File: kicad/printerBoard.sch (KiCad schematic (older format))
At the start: 24 parts, among them U1 POLOLU_A4988, U2 POLOLU_A4988

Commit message: Adding USL - sensors...
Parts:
- removed P?: CONN_01X04, symbol CONN_01X04
- added P?: CONN_01X05, symbol CONN_01X05
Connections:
- net ADIR is gone; now on net YDIR: U2.16 (DIR), U?.26 (PB13/SPI2_SCK/TIM1_CH1N/USART3_CTS)
- net AENABLE is gone; now on net YENABLE: U2.9 (EN), U?.22 (PB11/ADC1_EXTI11/ADC2_EXTI11/I2C2_SDA/TIM2_CH4/USART3_RX)
- net ASTEP is gone; now on net YSTEP: U2.15 (STEP), U?.25 (PB12/I2C2_SMBA/SPI2_NSS/TIM1_BKIN/USART3_CK)
- net Bpin1: no longer U?.11 (ADC1_IN1/ADC2_IN1/TIM2_CH2/USART2_RTS/PA1)
- net ULN12: no longer P?.2 (P2)
- net YDIR: no longer U?.16 (DIR), U?.20 (PB2/BOOT1)
- net YENABLE: no longer U?.45 (PB8/CAN_RX/I2C1_SCL/TIM4_CH3), U?.9 (EN)
- net YOUT1A: now also P?.2 (P2), U2.4 (1A); no longer U?.4 (1A)
- net YOUT1B: now also P?.1 (P1), U2.3 (IB); no longer U?.3 (IB)
- net YOUT2A: now also P?.3 (P3), U2.5 (2A); no longer U?.5 (2A)
- net YOUT2B: now also P?.4 (P4), U2.6 (2B); no longer U?.6 (2B)
- net YSTEP: no longer U?.15 (STEP), U?.21 (PB10/I2C2_SCL/TIM2_CH3/USART3_TX)
- net Zpin2: no longer U?.41 (PB5/I2C1_SMBA/SPI1_MOSI/TIM3_CH2)
- net Extruder_Sensor: now reaches U?.10 (ADC1_IN0/ADC2_IN0/SYS_WKUP/TIM2_CH1/TIM2_ETR/USART2_CTS/PA0)
- net Extruder_Sensor: now also P?.16 (P16)
- net PA13: now reaches U?.34 (SYS_JTMS-SWDIO/PA13)
- net PA13: now also U?.6 (I6)
- net PB1: now reaches U?.1 (I1)
- net Z5: now reaches U?.13 (O4)
- net Z5: now also P?.5 (P5)
- net Z4: now reaches U?.14 (O3)
- net Z4: now also P?.4 (P4)
- net Z2: now reaches U?.15 (O2)
- net Z2: now also P?.2 (P2)
- net Z1: now reaches U?.16 (O1)
- net Z1: now also P?.1 (P1)
- net PB0: now reaches U?.2 (I2)
- net PC13: now reaches U?.3 (I3)
- net PC14: now reaches U?.4 (I4)
- net PB14: now reaches U?.5 (I5)
- net Z3: now reaches U?.9 (COM)
- net Z3: now also P?.3 (P3)
- net SW_Y: now reaches P?.14 (P14)
- removed net AOUT1A: P?.2 (P2), P?.4 (P4), U2.4 (1A)
- removed net AOUT1B: P?.1 (P1), P?.3 (P3), U2.3 (IB)
- removed net AOUT2A: P?.3 (P3), P?.5 (P5), U2.5 (2A)
- removed net AOUT2B: P?.4 (P4), P?.6 (P6), U2.6 (2B)
- net Q1pin2 renamed Q1pin2-ExtruderHeater
- new net BedSensor: U?.11 (ADC1_IN1/ADC2_IN1/TIM2_CH2/USART2_RTS/PA1)
- new net EDIR: U?.16 (DIR)
- new net EENABLE: U?.9 (EN)
- new net EOUT1A: P?.4 (P4), U?.4 (1A)
- new net EOUT1B: P?.3 (P3), U?.3 (IB)
- new net EOUT2A: P?.5 (P5), U?.5 (2A)
- new net EOUT2B: P?.6 (P6), U?.6 (2B)
- new net ESTEP: U?.15 (STEP)
- new net ExtruderFAN: P?.2 (P2)
- new net SW_Z: U?.41 (PB5/I2C1_SMBA/SPI1_MOSI/TIM3_CH2)
- new net ZDIR: U?.20 (PB2/BOOT1)
- new net ZENABLE: U?.45 (PB8/CAN_RX/I2C1_SCL/TIM4_CH3)
- new net ZSTEP: U?.21 (PB10/I2C2_SCL/TIM2_CH3/USART3_TX)
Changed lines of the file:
@@
 XOUT1B
 Text GLabel 3450 6000 0    60   Input ~ 0
-AOUT1B
+YOUT1B
 Text GLabel 3450 6100 0    60   Input ~ 0
-AOUT1A
+YOUT1A
 Text GLabel 3450 6200 0    60   Input ~ 0
-AOUT2A
+YOUT2A
 Text GLabel 3450 6300 0    60   Input ~ 0
-AOUT2B
+YOUT2B
 Wire Wire Line
 	1450 6000 1550 6000
@@
 XOUT2B
 Text GLabel 3300 7000 0    60   Input ~ 0
-AOUT1B
+YOUT1B
 Text GLabel 3300 7100 0    60   Input ~ 0
-AOUT1A
+YOUT1A
 Text GLabel 3300 7200 0    60   Input ~ 0
-AOUT2A
+YOUT2A
 Text GLabel 3300 7300 0    60   Input ~ 0
-AOUT2B
+YOUT2B
 Text GLabel 1050 7400 0    60   Input ~ 0
 GND
@@
 	2950 6750 2950 6900
 Text GLabel 4700 6900 2    60   Input ~ 0
-ASTEP
+YSTEP
 Wire Wire Line
 	4600 6900 4700 6900
@@
 	2450 6800 2350 6800
 Text GLabel 4700 6800 2    60   Input ~ 0
-ADIR
+YDIR
 Text GLabel 1100 3900 0    60   Input ~ 0
-ASTEP
+YSTEP
 Text GLabel 1100 4000 0    60   Input ~ 0
-ADIR
+YDIR
 Wire Wire Line
 	1100 3900 1200 3900
@@
 XENABLE
 Text GLabel 1100 3800 0    60   Input ~ 0
-AENABLE
+YENABLE
 Wire Wire Line
 	7000 3500 7450 3500
@@
 $EndComp
 Text GLabel 4700 7500 2    60   Input ~ 0
-AENABLE
+YENABLE
 Wire Wire Line
 	4600 7500 4700 7500
@@
 Wire Wire Line
 	5400 7200 5450 7200
-$Comp
-L CONN_01X04 P?
-U 1 1 5A502458
-P 4800 6100
-F 0 "P?" H 4800 6350 50  0000 C CNN
-F 1 "CONN_01X04" V 4900 6100 50  0000 C CNN
-F 2 "" H 4800 6100 50  0000 C CNN
-F 3 "" H 4800 6100 50  0000 C CNN
-	1    4800 6100
-	1    0    0    -1
-$EndComp
 Text GLabel 6700 7200 2    60   Input ~ 0
-YENABLE
+EENABLE
 Wire Wire Line
 	6650 7200 6700 7200
@@
 Connection ~ 6750 6800
 Text GLabel 6700 6600 2    60   Input ~ 0
-YSTEP
+ESTEP
 Text GLabel 6700 6500 2    60   Input ~ 0
-YDIR
+EDIR
 Wire Wire Line
 	6650 6500 6700 6500
@@
 GND
 Text GLabel 5400 7000 0    60   Input ~ 0
-YOUT2B
+EOUT2B
 Text GLabel 5400 6900 0    60   Input ~ 0
-YOUT2A
+EOUT2A
 Text GLabel 5400 6800 0    60   Input ~ 0
-YOUT1A
+EOUT1A
 Text GLabel 5400 6700 0    60   Input ~ 0
-YOUT1B
+EOUT1B
 Text GLabel 5400 6500 0    60   Input ~ 0
 GND
@@
 	5400 7100 5450 7100
 Text GLabel 1100 2900 0    60   Input ~ 0
-YDIR
+ZDIR
 Text GLabel 1100 3700 0    60   Input ~ 0
-YSTEP
+ZSTEP
 Wire Wire Line
 	1100 2900 1200 2900
@@
 	1100 3700 1200 3700
 Text GLabel 1100 3500 0    60   Input ~ 0
-YENABLE
+ZENABLE
 Wire Wire Line
 	1100 3500 1200 3500
 Text GLabel 5650 5800 3    60   Input ~ 0
-AOUT2A
+EOUT2A
 Text GLabel 5550 5800 3    60   Input ~ 0
-AOUT1A
+EOUT1A
 Wire Wire Line
 	5550 5700 5550 5800
@@
 	5250 5700 5250 5800
 Text GLabel 5450 5800 3    60   Input ~ 0
-AOUT1B
+EOUT1B
 Text GLabel 5750 5800 3    60   Input ~ 0
-AOUT2B
+EOUT2B
 Wire Wire Line
 	5450 5800 5450 5700
@@
 	5750 5800 5750 5700
 Text GLabel 5350 5800 3    60   Input ~ 0
-ULN12
+ExtruderFAN
 Wire Wire Line
 	5350 5700 5350 5800
@@
 Connection ~ 6250 5750
 Text GLabel 6250 5800 3    60   Input ~ 0
-Q1pin2
+Q1pin2-ExtruderHeater
 Text GLabel 6650 5800 3    60   Input ~ 0
 GND
@@
 	700  3400 800  3400
 Text GLabel 1050 3200 0    60   Input ~ 0
-Zpin2
+SW_Z
 Wire Wire Line
 	1050 3200 1200 3200
@@
 	1950 4950 2100 4950
 Text GLabel 7450 2800 2    60   Input ~ 0
-Bpin1
+BedSensor
 Wire Wire Line
 	7000 2800 7450 2800
@@
 Wire Wire Line
 	1050 3100 1200 3100
+Text GLabel 6550 5800 3    60   Input ~ 0
+SW_Y
+Wire Wire Line
+	6550 5800 6550 5700
+Text GLabel 6750 5800 3    60   Input ~ 0
+Extruder_Sensor
+Wire Wire Line
+	6750 5800 6750 5700
+Text GLabel 7450 2700 2    60   Input ~ 0
+Extruder_Sensor
+Wire Wire Line
+	7000 2700 7450 2700
+$Comp
+L CONN_01X05 P?
+U 1 1 5A5C0404
+P 4700 6000
+F 0 "P?" H 4700 6300 50  0000 C CNN
+F 1 "CONN_01X05" V 4800 6000 50  0000 C CNN
+F 2 "" H 4700 6000 50  0000 C CNN
+F 3 "" H 4700 6000 50  0000 C CNN
+	1    4700 6000
+	1    0    0    -1
+$EndComp
+Text GLabel 4400 5800 0    60   Input ~ 0
+Z1
+Text GLabel 4400 5900 0    60   Input ~ 0
+Z2
+Text GLabel 4400 6000 0    60   Input ~ 0
+Z3
+Text GLabel 4400 6100 0    60   Input ~ 0
+Z4
+Text GLabel 4400 6200 0    60   Input ~ 0
+Z5
+Wire Wire Line
+	4400 5800 4500 5800
+Wire Wire Line
+	4400 5900 4500 5900
+Wire Wire Line
+	4400 6000 4500 6000
+Wire Wire Line
+	4400 6100 4500 6100
+Wire Wire Line
+	4400 6200 4500 6200
+Text GLabel 9150 1000 2    60   Input ~ 0
+Z1
+Wire Wire Line
+	9000 1000 9150 1000
+Text GLabel 9150 1100 2    60   Input ~ 0
+Z2
+Text GLabel 9150 1800 2    60   Input ~ 0
+Z3
+Text GLabel 9150 1200 2    60   Input ~ 0
+Z4
+Wire Wire Line
+	9000 1100 9150 1100
+Wire Wire Line
+	9000 1200 9150 1200
+Wire Wire Line
+	9150 1800 9000 1800
+Text GLabel 9150 1300 2    60   Input ~ 0
+Z5
+Wire Wire Line
+	9000 1300 9150 1300
+Text GLabel 7550 1000 0    60   Input ~ 0
+PB1
+Text GLabel 7550 1100 0    60   Input ~ 0
+PB0
+Text GLabel 7550 1200 0    60   Input ~ 0
+PC13
+Text GLabel 7550 1300 0    60   Input ~ 0
+PC14
+Text GLabel 7550 1400 0    60   Input ~ 0
+PB14
+Text GLabel 7550 1500 0    60   Input ~ 0
+PA13
+Wire Wire Line
+	7550 1000 7700 1000
+Wire Wire Line
+	7550 1100 7700 1100
+Wire Wire Line
+	7550 1200 7700 1200
+Wire Wire Line
+	7550 1300 7700 1300
+Wire Wire Line
+	7550 1400 7700 1400
+Wire Wire Line
+	7550 1500 7700 1500
+Text GLabel 7450 4000 2    60   Input ~ 0
+PA13
+Wire Wire Line
+	7000 4000 7450 4000
 $EndSCHEMATC

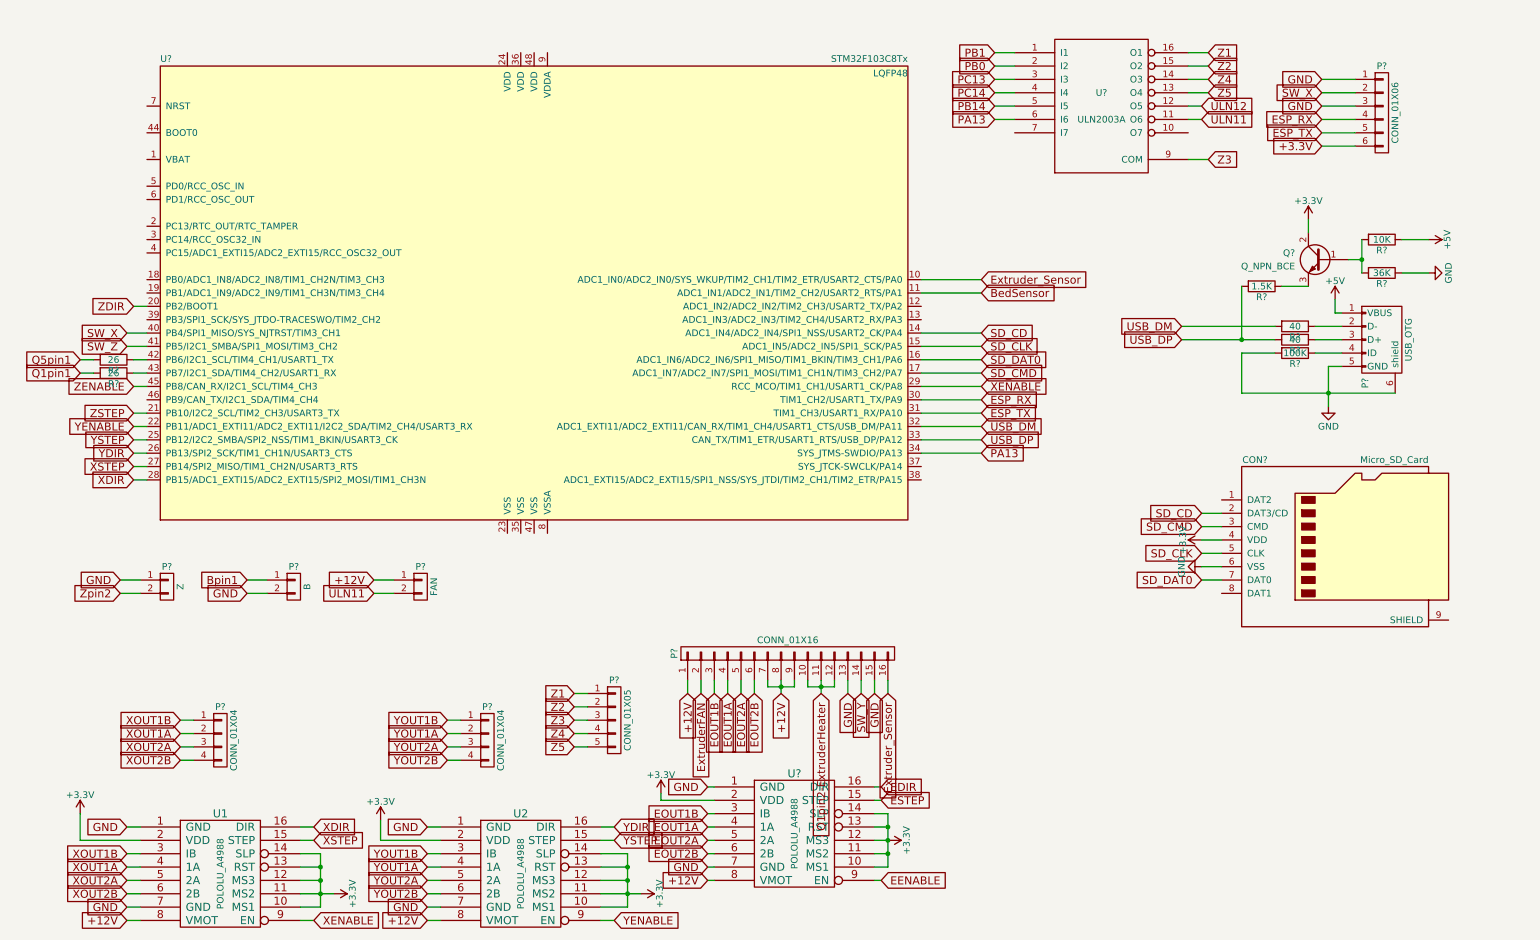
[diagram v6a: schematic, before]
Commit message: Adding some more fix USB
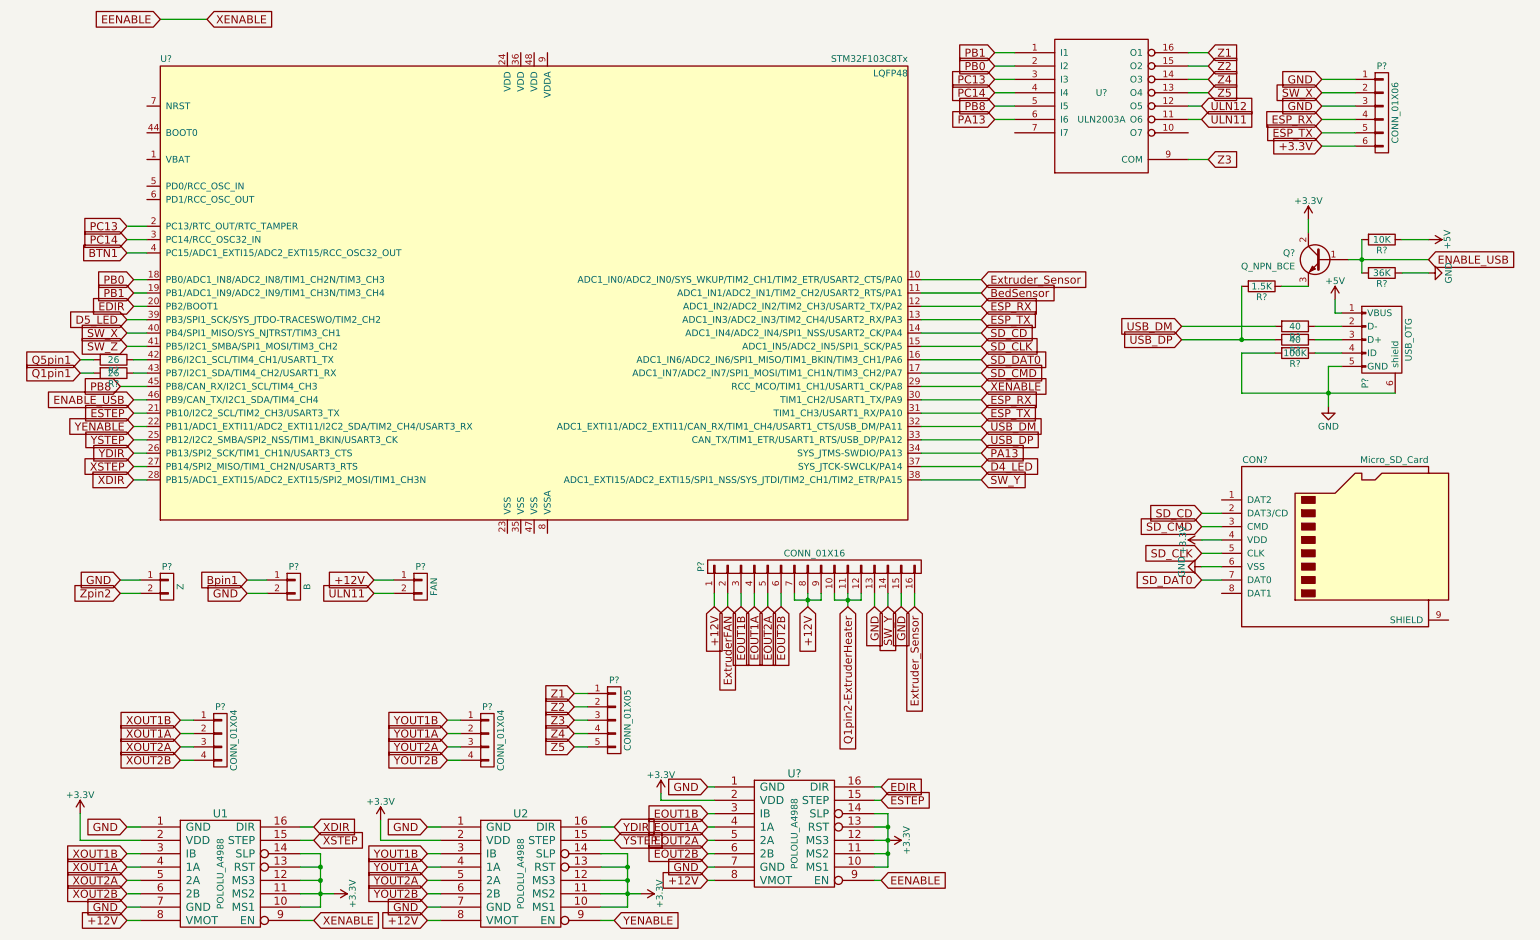
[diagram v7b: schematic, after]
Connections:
- net XENABLE is gone; now on net EENABLE: U1.9 (EN), U?.29 (RCC_MCO/TIM1_CH1/USART1_CK/PA8)
- net ZDIR is gone; now on net EDIR: U?.20 (PB2/BOOT1)
- net ZENABLE is gone; now on net PB8: U?.45 (PB8/CAN_RX/I2C1_SCL/TIM4_CH3)
- net ZSTEP is gone; now on net ESTEP: U?.21 (PB10/I2C2_SCL/TIM2_CH3/USART3_TX)
- net ESP_RX: now also U?.12 (ADC1_IN2/ADC2_IN2/TIM2_CH3/USART2_TX/PA2)
- net ESP_TX: now also U?.13 (ADC1_IN3/ADC2_IN3/TIM2_CH4/USART2_RX/PA3)
- net PB0: now also U?.18 (PB0/ADC1_IN8/ADC2_IN8/TIM1_CH2N/TIM3_CH3)
- net PB1: now also U?.19 (PB1/ADC1_IN9/ADC2_IN9/TIM1_CH3N/TIM3_CH4)
- net PC13: now also U?.2 (PC13/RTC_OUT/RTC_TAMPER)
- net PC14: now also U?.3 (PC14/RCC_OSC32_IN)
- net SW_Y: now also U?.38 (ADC1_EXTI15/ADC2_EXTI15/SPI1_NSS/SYS_JTDI/TIM2_CH1/TIM2_ETR/PA15)
- net D4_LED: now reaches U?.37 (SYS_JTCK-SWCLK/PA14)
- net D5_LED: now reaches U?.39 (PB3/SPI1_SCK/SYS_JTDO-TRACESWO/TIM2_CH2)
- net BTN1: now reaches U?.4 (PC15/ADC1_EXTI15/ADC2_EXTI15/RCC_OSC32_OUT)
- net ENABLE_USB: now reaches U?.46 (PB9/CAN_TX/I2C1_SDA/TIM4_CH4)
- net ENABLE_USB: now also Q?.1 (B), R?.2, R?.2
- net PB14 renamed PB8
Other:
- moved on the sheet: P?
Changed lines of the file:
@@
 $EndComp
 Wire Wire Line
-	10200 2550 10300 2550
+	10200 2550 10800 2550
 Wire Wire Line
 	10300 2400 10300 2650
@@
 Text GLabel 3300 6800 0    60   Input ~ 0
 GND
-Text GLabel 6450 5800 3    60   Input ~ 0
+Text GLabel 6650 5150 3    60   Input ~ 0
 GND
 $Comp
@@
 L CONN_01X16 P?
 U 1 1 5A4EABEF
-P 6000 5500
-F 0 "P?" H 6000 6350 50  0000 C CNN
-F 1 "CONN_01X16" V 6100 5500 50  0000 C CNN
-F 2 "" H 6000 5500 50  0000 C CNN
-F 3 "" H 6000 5500 50  0000 C CNN
-	1    6000 5500
+P 6200 4850
+F 0 "P?" H 6200 5700 50  0000 C CNN
+F 1 "CONN_01X16" V 6300 4850 50  0000 C CNN
+F 2 "" H 6200 4850 50  0000 C CNN
+F 3 "" H 6200 4850 50  0000 C CNN
+	1    6200 4850
 	0    -1   -1   0
 $EndComp
-Text GLabel 5250 5800 3    60   Input ~ 0
+Text GLabel 5450 5150 3    60   Input ~ 0
 +12V
 Text GLabel 1050 7500 0    60   Input ~ 0
@@
 	5400 7100 5450 7100
 Text GLabel 1100 2900 0    60   Input ~ 0
-ZDIR
+EDIR
 Text GLabel 1100 3700 0    60   Input ~ 0
-ZSTEP
+ESTEP
 Wire Wire Line
 	1100 2900 1200 2900
 Wire Wire Line
 	1100 3700 1200 3700
-Text GLabel 1100 3500 0    60   Input ~ 0
-ZENABLE
-Wire Wire Line
-	1100 3500 1200 3500
-Text GLabel 5650 5800 3    60   Input ~ 0
+Text GLabel 1300 750  0    60   Input ~ 0
+EENABLE
+Wire Wire Line
+	1000 3500 1200 3500
+Text GLabel 5850 5150 3    60   Input ~ 0
 EOUT2A
-Text GLabel 5550 5800 3    60   Input ~ 0
+Text GLabel 5750 5150 3    60   Input ~ 0
 EOUT1A
 Wire Wire Line
-	5550 5700 5550 5800
-Wire Wire Line
-	5650 5700 5650 5800
-Wire Wire Line
-	5250 5700 5250 5800
-Text GLabel 5450 5800 3    60   Input ~ 0
+	5750 5050 5750 5150
+Wire Wire Line
+	5850 5050 5850 5150
+Wire Wire Line
+	5450 5050 5450 5150
+Text GLabel 5650 5150 3    60   Input ~ 0
 EOUT1B
-Text GLabel 5750 5800 3    60   Input ~ 0
+Text GLabel 5950 5150 3    60   Input ~ 0
 EOUT2B
 Wire Wire Line
-	5450 5800 5450 5700
-Wire Wire Line
-	5750 5800 5750 5700
-Text GLabel 5350 5800 3    60   Input ~ 0
+	5650 5150 5650 5050
+Wire Wire Line
+	5950 5150 5950 5050
+Text GLabel 5550 5150 3    60   Input ~ 0
 ExtruderFAN
 Wire Wire Line
-	5350 5700 5350 5800
+	5550 5050 5550 5150
 Text GLabel 9100 1500 2    60   Input ~ 0
 ULN11
@@
 	9000 1500 9100 1500
 Wire Wire Line
-	5850 5700 5850 5750
-Wire Wire Line
-	5850 5750 6050 5750
-Wire Wire Line
-	5950 5700 5950 5800
-Text GLabel 5950 5800 3    60   Input ~ 0
+	6050 5050 6050 5100
+Wire Wire Line
+	6050 5100 6250 5100
+Wire Wire Line
+	6150 5050 6150 5150
+Text GLabel 6150 5150 3    60   Input ~ 0
 +12V
-Connection ~ 5950 5750
-Wire Wire Line
-	6050 5750 6050 5700
-Wire Wire Line
-	6150 5700 6150 5750
-Wire Wire Line
-	6150 5750 6350 5750
-Wire Wire Line
-	6350 5750 6350 5700
-Wire Wire Line
-	6250 5700 6250 5800
-Connection ~ 6250 5750
-Text GLabel 6250 5800 3    60   Input ~ 0
+Connection ~ 6150 5100
+Wire Wire Line
+	6250 5100 6250 5050
+Wire Wire Line
+	6350 5050 6350 5100
+Wire Wire Line
+	6350 5100 6550 5100
+Wire Wire Line
+	6550 5100 6550 5050
+Wire Wire Line
+	6450 5050 6450 5150
+Connection ~ 6450 5100
+Text GLabel 6450 5150 3    60   Input ~ 0
 Q1pin2-ExtruderHeater
-Text GLabel 6650 5800 3    60   Input ~ 0
-GND
-Wire Wire Line
-	6650 5800 6650 5700
-Wire Wire Line
-	6450 5700 6450 5800
+Text GLabel 6850 5150 3    60   Input ~ 0
+GND
+Wire Wire Line
+	6850 5150 6850 5050
+Wire Wire Line
+	6650 5050 6650 5150
 $Comp
 L R R?
@@
 Wire Wire Line
 	1050 3100 1200 3100
-Text GLabel 6550 5800 3    60   Input ~ 0
+Text GLabel 6750 5150 3    60   Input ~ 0
 SW_Y
 Wire Wire Line
-	6550 5800 6550 5700
-Text GLabel 6750 5800 3    60   Input ~ 0
+	6750 5150 6750 5050
+Text GLabel 6950 5150 3    60   Input ~ 0
 Extruder_Sensor
 Wire Wire Line
-	6750 5800 6750 5700
+	6950 5150 6950 5050
 Text GLabel 7450 2700 2    60   Input ~ 0
 Extruder_Sensor
@@
 PC14
 Text GLabel 7550 1400 0    60   Input ~ 0
-PB14
+PB8
 Text GLabel 7550 1500 0    60   Input ~ 0
 PA13
@@
 Wire Wire Line
 	7000 4000 7450 4000
+Text GLabel 1100 2700 0    60   Input ~ 0
+PB0
+Text GLabel 1100 2800 0    60   Input ~ 0
+PB1
+Text GLabel 1050 2300 0    60   Input ~ 0
+PC13
+Text GLabel 1050 2400 0    60   Input ~ 0
+PC14
+Wire Wire Line
+	1050 2300 1200 2300
+Wire Wire Line
+	1050 2400 1200 2400
+Wire Wire Line
+	1100 2700 1200 2700
+Wire Wire Line
+	1100 2800 1200 2800
+Text GLabel 1000 3500 0    60   Input ~ 0
+PB8
+Text GLabel 1650 750  2    60   Input ~ 0
+XENABLE
+Wire Wire Line
+	1300 750  1650 750
+Text GLabel 7450 3000 2    60   Input ~ 0
+ESP_TX
+Text GLabel 7450 2900 2    60   Input ~ 0
+ESP_RX
+Wire Wire Line
+	7000 2900 7450 2900
+Wire Wire Line
+	7000 3000 7450 3000
+Text GLabel 7450 4100 2    60   Input ~ 0
+D4_LED
+Wire Wire Line
+	7000 4100 7450 4100
+Text GLabel 1050 2500 0    60   Input ~ 0
+BTN1
+Wire Wire Line
+	1050 2500 1200 2500
+Text GLabel 7450 4200 2    60   Input ~ 0
+SW_Y
+Wire Wire Line
+	7000 4200 7450 4200
+Text GLabel 1050 3000 0    60   Input ~ 0
+D5_LED
+Wire Wire Line
+	1050 3000 1200 3000
+Text GLabel 1100 3600 0    60   Input ~ 0
+ENABLE_USB
+Wire Wire Line
+	1100 3600 1200 3600
+Text GLabel 10800 2550 2    60   Input ~ 0
+ENABLE_USB
 $EndSCHEMATC
